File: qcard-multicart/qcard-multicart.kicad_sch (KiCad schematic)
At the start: 12 parts, among them J1 Conn_02x18_Top_Bottom, SW1 SW_DIP_x04, U1 MX29LV640EBTI-70G, U2 MIC5365-3.3YD5

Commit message: WIP
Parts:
- added RN1, RN2, RN3, RN4: 2K, reb-r-array:EXB2HV202JV, symbol Device:R_Pack08
- C1, C2, C3: symbol Device:C -> Device:C_Small
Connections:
- net A0: now also RN1.13 (R4.2); no longer J1.13 (Pin_13)
- net A1: now also RN1.12 (R5.2); no longer J1.12 (Pin_12)
- net A10: now also RN3.10 (R7.2); no longer J1.28 (Pin_28)
- net A11: now also RN4.16 (R1.2); no longer J1.26 (Pin_26)
- net A12: now also RN2.13 (R4.2); no longer J1.5 (Pin_5)
- net A13: now also RN4.13 (R4.2); no longer J1.23 (Pin_23)
- net A14: now also RN4.12 (R5.2); no longer J1.22 (Pin_22)
- net A15: now also RN2.12 (R5.2); no longer J1.4 (Pin_4)
- net A16: now also RN2.11 (R6.2); no longer J1.3 (Pin_3)
- net A17: now also RN4.11 (R6.2); no longer J1.21 (Pin_21)
- net A18: now also RN4.10 (R7.2); no longer J1.20 (Pin_20)
- net A2: now also RN1.11 (R6.2); no longer J1.11 (Pin_11)
- net A3: now also RN1.10 (R7.2); no longer J1.10 (Pin_10)
- net A4: now also RN1.9 (R8.2); no longer J1.9 (Pin_9)
- net A5: now also RN2.16 (R1.2); no longer J1.8 (Pin_8)
- net A6: now also RN2.15 (R2.2); no longer J1.7 (Pin_7)
- net A7: now also RN2.14 (R3.2); no longer J1.6 (Pin_6)
- net A8: now also RN4.14 (R3.2); no longer J1.24 (Pin_24)
- net A9: now also RN4.15 (R2.2); no longer J1.25 (Pin_25)
- net CE: now also RN3.11 (R6.2); no longer J1.29 (Pin_29)
- net D0: now also RN1.14 (R3.2); no longer J1.14 (Pin_14)
- net D1: now also RN1.15 (R2.2); no longer J1.15 (Pin_15)
- net D2: now also RN1.16 (R1.2); no longer J1.16 (Pin_16)
- net D3: now also RN3.16 (R1.2); no longer J1.34 (Pin_34)
- net D4: now also RN3.15 (R2.2); no longer J1.33 (Pin_33)
- net D5: now also RN3.14 (R3.2); no longer J1.32 (Pin_32)
- net D6: now also RN3.13 (R4.2); no longer J1.31 (Pin_31)
- net D7: now also RN3.12 (R5.2); no longer J1.30 (Pin_30)
- net OE: now also RN3.9 (R8.2); no longer J1.27 (Pin_27)
- net at SW1.5, U1.16 (A18): now also R5.2; no longer R2.2
- net at SW1.7, U1.10 (A20): now also R3.2; no longer R4.2
- net at SW1.6, U1.9 (A19): now also R4.2; no longer R3.2
- net at SW1.8, U1.13 (A21): now also R2.2; no longer R5.2
- new net: J1.8 (Pin_8), RN2.1 (R1.1)
- new net: J1.7 (Pin_7), RN2.2 (R2.1)
- new net: J1.6 (Pin_6), RN2.3 (R3.1)
- new net: J1.5 (Pin_5), RN2.4 (R4.1)
- new net: J1.4 (Pin_4), RN2.5 (R5.1)
- new net: J1.3 (Pin_3), RN2.6 (R6.1)
- new net: J1.26 (Pin_26), RN4.1 (R1.1)
- new net: J1.25 (Pin_25), RN4.2 (R2.1)
- new net: J1.24 (Pin_24), RN4.3 (R3.1)
- new net: J1.23 (Pin_23), RN4.4 (R4.1)
- new net: J1.22 (Pin_22), RN4.5 (R5.1)
- new net: J1.21 (Pin_21), RN4.6 (R6.1)
- new net: J1.20 (Pin_20), RN4.7 (R7.1)
- new net: J1.10 (Pin_10), RN1.7 (R7.1)
- new net: J1.11 (Pin_11), RN1.6 (R6.1)
- new net: J1.12 (Pin_12), RN1.5 (R5.1)
- new net: J1.13 (Pin_13), RN1.4 (R4.1)
- new net: J1.14 (Pin_14), RN1.3 (R3.1)
- new net: J1.15 (Pin_15), RN1.2 (R2.1)
- new net: J1.16 (Pin_16), RN1.1 (R1.1)
- new net: J1.27 (Pin_27), RN3.8 (R8.1)
- new net: J1.28 (Pin_28), RN3.7 (R7.1)
- new net: J1.29 (Pin_29), RN3.6 (R6.1)
- new net: J1.30 (Pin_30), RN3.5 (R5.1)
- new net: J1.31 (Pin_31), RN3.4 (R4.1)
- new net: J1.32 (Pin_32), RN3.3 (R3.1)
- new net: J1.33 (Pin_33), RN3.2 (R2.1)
- new net: J1.34 (Pin_34), RN3.1 (R1.1)
- new net: J1.9 (Pin_9), RN1.8 (R8.1)
- no-connect marks 8 -> 14
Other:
- note added: "TODO: Put R in front of all logic lines"
- moved on the sheet: C3, J1, R2, R3, R4, R5

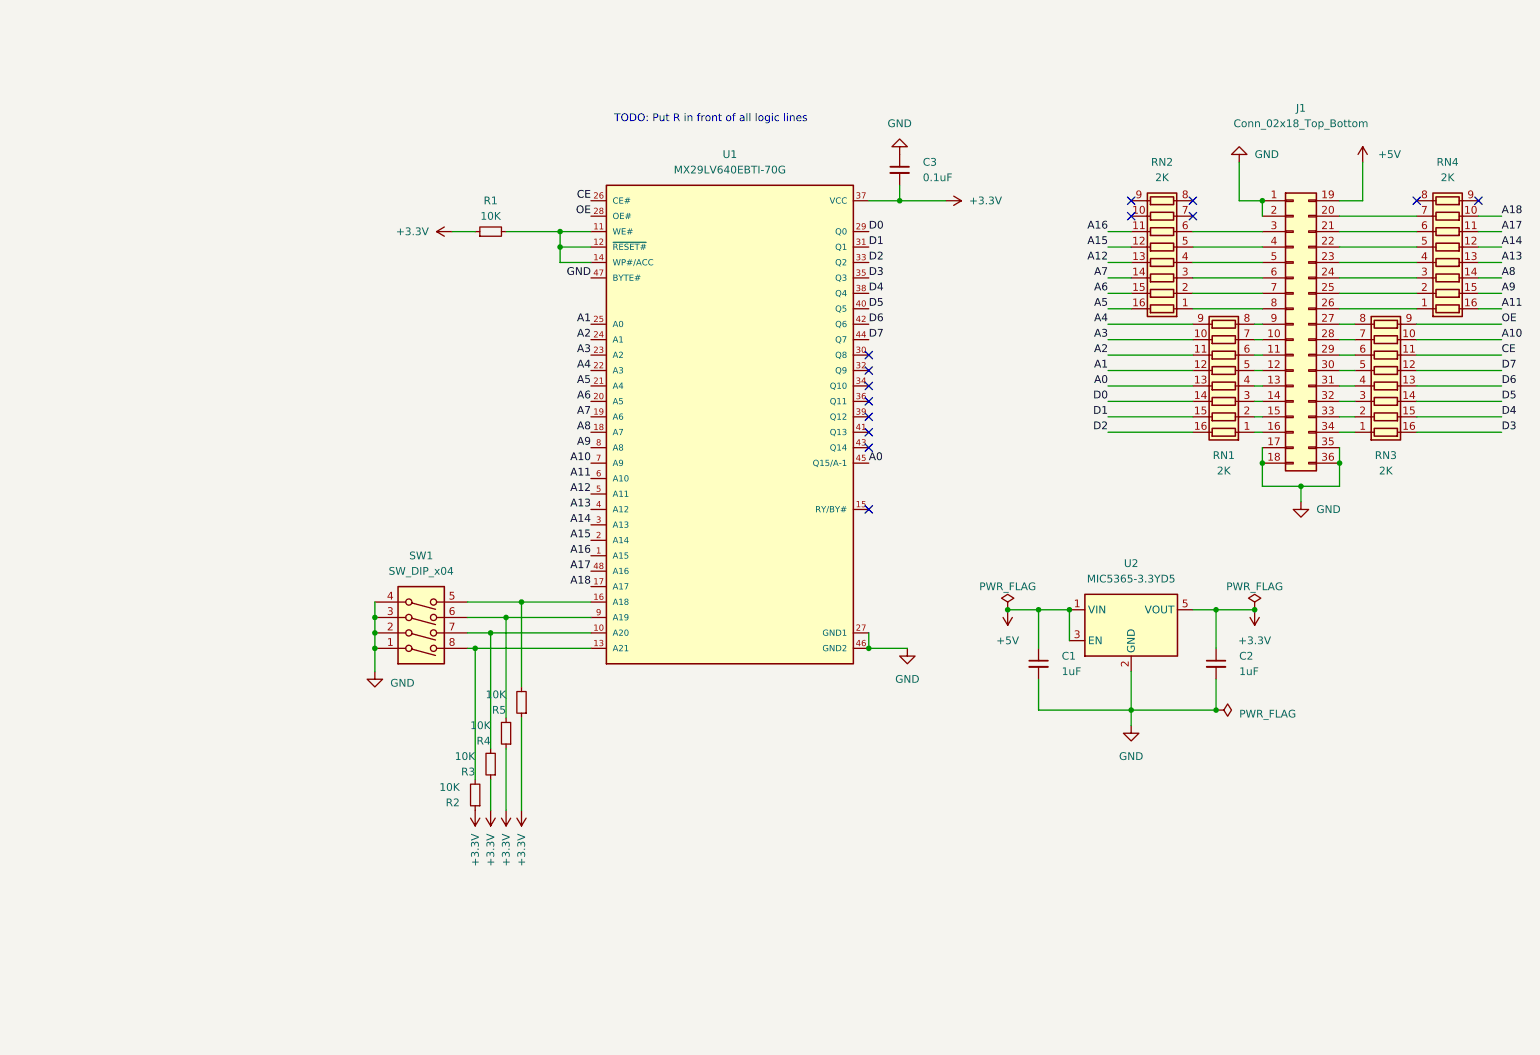
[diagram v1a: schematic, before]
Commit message: Adds staggered RNs (painstakingly)
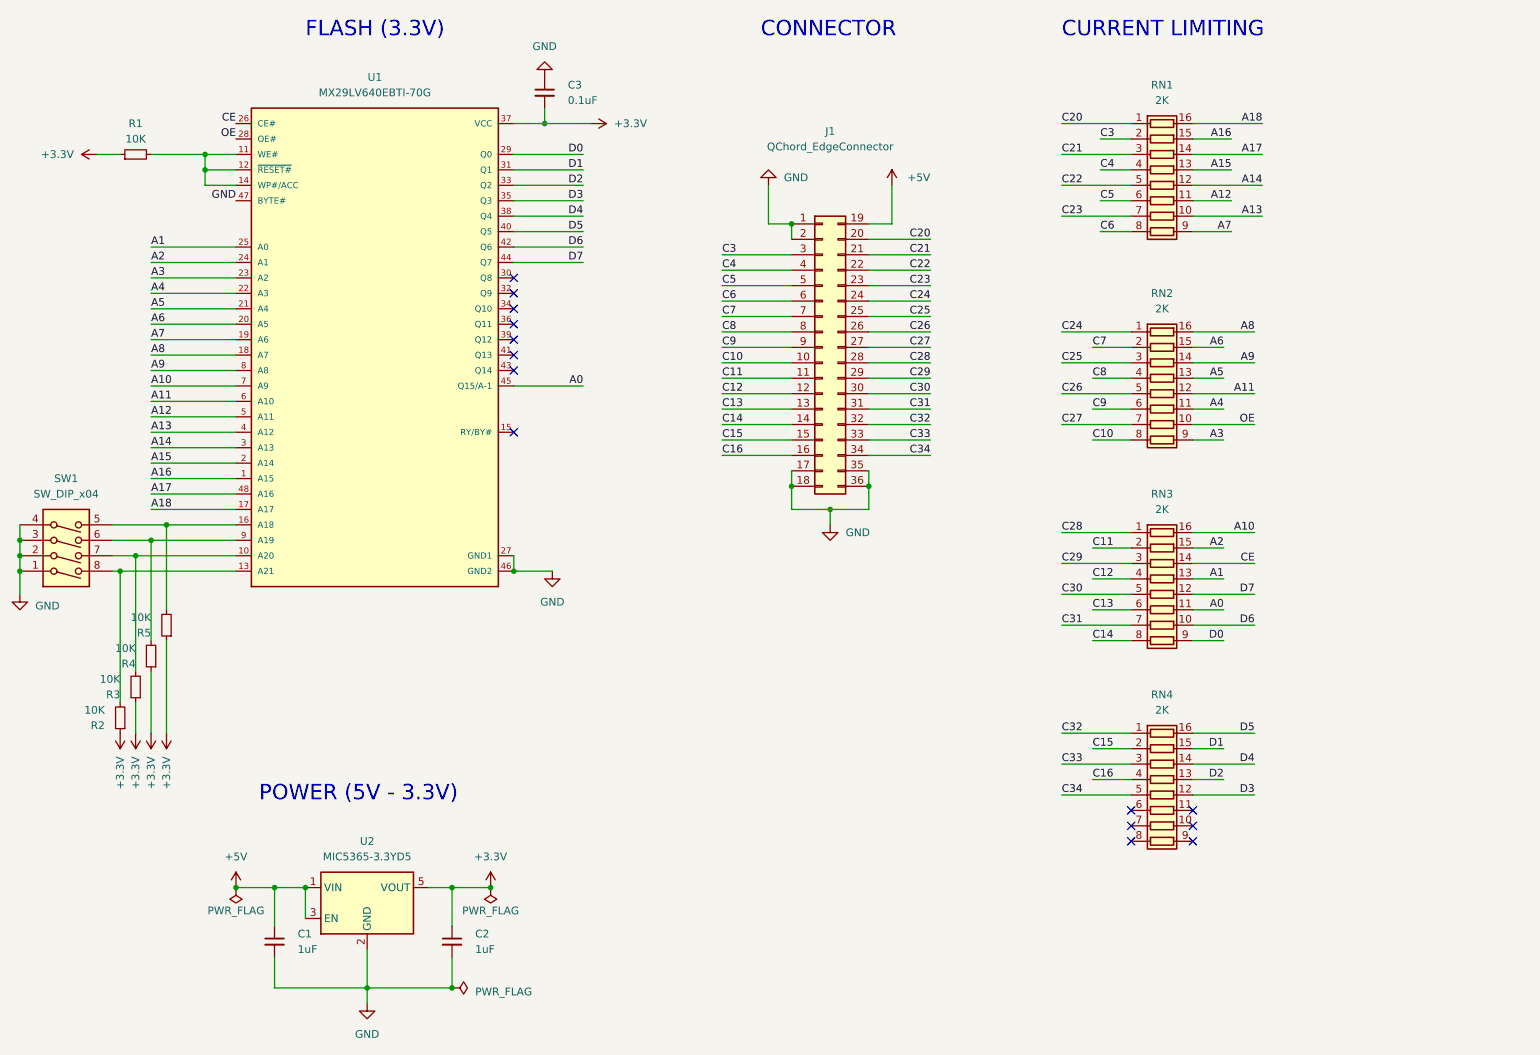
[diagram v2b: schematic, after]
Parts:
- J1: value Conn_02x18_Top_Bottom -> QChord_EdgeConnector
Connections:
- net A0: now also RN3.11 (R6.2); no longer RN1.13 (R4.2)
- net A1: now also RN3.13 (R4.2); no longer RN1.12 (R5.2)
- net A10: now also RN3.16 (R1.2); no longer RN3.10 (R7.2)
- net A11: now also RN2.12 (R5.2); no longer RN4.16 (R1.2)
- net A12: now also RN1.11 (R6.2); no longer RN2.13 (R4.2)
- net A13: now also RN1.10 (R7.2); no longer RN4.13 (R4.2)
- net A14: now also RN1.12 (R5.2); no longer RN4.12 (R5.2)
- net A15: now also RN1.13 (R4.2); no longer RN2.12 (R5.2)
- net A16: now also RN1.15 (R2.2); no longer RN2.11 (R6.2)
- net A17: now also RN1.14 (R3.2); no longer RN4.11 (R6.2)
- net A18: now also RN1.16 (R1.2); no longer RN4.10 (R7.2)
- net A2: now also RN3.15 (R2.2); no longer RN1.11 (R6.2)
- net A3: now also RN2.9 (R8.2); no longer RN1.10 (R7.2)
- net A4: now also RN2.11 (R6.2); no longer RN1.9 (R8.2)
- net A5: now also RN2.13 (R4.2); no longer RN2.16 (R1.2)
- net A7: now also RN1.9 (R8.2); no longer RN2.14 (R3.2)
- net A8: now also RN2.16 (R1.2); no longer RN4.14 (R3.2)
- net A9: now also RN2.14 (R3.2); no longer RN4.15 (R2.2)
- net CE: now also RN3.14 (R3.2); no longer RN3.11 (R6.2)
- net D0: now also RN3.9 (R8.2); no longer RN1.14 (R3.2)
- net D1: now also RN4.15 (R2.2); no longer RN1.15 (R2.2)
- net D2: now also RN4.13 (R4.2); no longer RN1.16 (R1.2)
- net D3: now also RN4.12 (R5.2); no longer RN3.16 (R1.2)
- net D4: now also RN4.14 (R3.2); no longer RN3.15 (R2.2)
- net D5: now also RN4.16 (R1.2); no longer RN3.14 (R3.2)
- net D6: now also RN3.10 (R7.2); no longer RN3.13 (R4.2)
- net OE: now also RN2.10 (R7.2); no longer RN3.9 (R8.2)
- net C24: now reaches RN2.1 (R1.1)
- net C24: now also J1.24 (Pin_24); no longer J1.8 (Pin_8)
- net C7: now reaches J1.7 (Pin_7), RN2.2 (R2.1)
- net C25: now reaches RN2.3 (R3.1)
- net C25: now also J1.25 (Pin_25); no longer J1.6 (Pin_6)
- net C5: now reaches J1.5 (Pin_5)
- net C5: now also RN1.6 (R6.1); no longer RN2.4 (R4.1)
- net C26: now reaches RN2.5 (R5.1)
- net C26: now also J1.26 (Pin_26); no longer J1.4 (Pin_4)
- net C3: now reaches J1.3 (Pin_3)
- net C3: now also RN1.2 (R2.1); no longer RN2.6 (R6.1)
- net C27: now reaches RN2.7 (R7.1)
- net C27: now also J1.27 (Pin_27)
- net C10: now reaches RN2.8 (R8.1)
- net C10: now also J1.10 (Pin_10)
- net C32: now reaches RN4.1 (R1.1)
- net C32: now also J1.32 (Pin_32); no longer J1.26 (Pin_26)
- net C15: now reaches RN4.2 (R2.1)
- net C15: now also J1.15 (Pin_15); no longer J1.25 (Pin_25)
- net C33: now reaches RN4.3 (R3.1)
- net C33: now also J1.33 (Pin_33); no longer J1.24 (Pin_24)
- net C16: now reaches RN4.4 (R4.1)
- net C16: now also J1.16 (Pin_16); no longer J1.23 (Pin_23)
- net C22: now reaches J1.22 (Pin_22)
- net C22: now also RN1.5 (R5.1); no longer RN4.5 (R5.1)
- net at RN4.6 (R6.1): no longer J1.21 (Pin_21)
- net at RN4.7 (R7.1): no longer J1.20 (Pin_20)
- net C23: now reaches RN1.7 (R7.1)
- net C23: now also J1.23 (Pin_23); no longer J1.10 (Pin_10)
- net C11: now reaches J1.11 (Pin_11)
- net C11: now also RN3.2 (R2.1); no longer RN1.6 (R6.1)
- net C12: now reaches J1.12 (Pin_12)
- net C12: now also RN3.4 (R4.1); no longer RN1.5 (R5.1)
- net C13: now reaches J1.13 (Pin_13)
- net C13: now also RN3.6 (R6.1); no longer RN1.4 (R4.1)
- net C14: now reaches J1.14 (Pin_14)
- net C14: now also RN3.8 (R8.1); no longer RN1.3 (R3.1)
- net C20: now reaches RN1.1 (R1.1)
- net C20: now also J1.20 (Pin_20); no longer J1.16 (Pin_16)
- net C28: now reaches J1.28 (Pin_28)
- net C28: now also RN3.1 (R1.1); no longer RN3.7 (R7.1)
- net C29: now reaches J1.29 (Pin_29)
- net C29: now also RN3.3 (R3.1); no longer RN3.6 (R6.1)
- net C30: now reaches J1.30 (Pin_30), RN3.5 (R5.1)
- net C31: now reaches J1.31 (Pin_31)
- net C31: now also RN3.7 (R7.1); no longer RN3.4 (R4.1)
- net C34: now reaches J1.34 (Pin_34)
- net C34: now also RN4.5 (R5.1); no longer RN3.1 (R1.1)
- net C6: now reaches RN1.8 (R8.1)
- net C6: now also J1.6 (Pin_6); no longer J1.9 (Pin_9)
- new net C21: J1.21 (Pin_21), RN1.3 (R3.1)
- new net C4: J1.4 (Pin_4), RN1.4 (R4.1)
- new net C8: J1.8 (Pin_8), RN2.4 (R4.1)
- new net C9: J1.9 (Pin_9), RN2.6 (R6.1)
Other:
- note added: "CONNECTOR"
- note added: "CURRENT LIMITING"
- note added: "FLASH (3.3V)"
- note added: "POWER (5V - 3.3V)"
- note removed: "TODO: Put R in front of all logic lines"
- moved on the sheet: C1, C2, C3, J1, R1, R2, R3, R4, R5, SW1, U1, U2
